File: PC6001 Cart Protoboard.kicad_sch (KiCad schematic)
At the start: 16 parts, among them J1 PC-6001 edge connector, SW1 PicoReset, SW2 EspReset, SW3 Button A, U2 ESP32-DevKitC, U3 74LS32, U4 microSD-Breakout

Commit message: oopsie on '08
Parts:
- removed unit 1 of U3
- added U5: 74LS08, Package_DIP:DIP-14_W7.62mm_Socket_LongPads, symbol 74xx:74LS08
- U3: footprint (none) -> Package_DIP:DIP-14_W7.62mm_Socket_LongPads
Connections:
- net +5V: now also U5.14 (VCC)
- net GND: now also U5.7 (GND)
- net ~{CS2}: now also U5.2
- net ~{CS3}: now also U5.1
- net ~{ROMSEL}: now also U5.3
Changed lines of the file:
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@@
 	)
 	(junction
+		(at 90.17 187.96)
+		(diameter 0)
+		(color 0 0 0 0)
+	)
+	(junction
 		(at 185.42 39.37)
 		(diameter 0)
@@
 	)
 	(junction
+		(at 90.17 162.56)
+		(diameter 0)
+		(color 0 0 0 0)
+	)
+	(junction
 		(at 226.06 53.34)
 		(diameter 0)
@@
 	(wire
 		(pts
+			(xy 69.85 187.96) (xy 90.17 187.96)
+		)
+		(stroke
+			(width 0)
+			(type default)
+		)
+	)
+	(wire
+		(pts
 			(xy 242.57 123.19) (xy 252.73 123.19)
 		)
@@
 	(wire
 		(pts
+			(xy 69.85 162.56) (xy 90.17 162.56)
+		)
+		(stroke
+			(width 0)
+			(type default)
+		)
+	)
+	(wire
+		(pts
 			(xy 177.8 29.21) (xy 185.42 29.21)
 		)
@@
 			)
 		)
-		(property "Footprint" ""
+		(property "Footprint" "Package_DIP:DIP-14_W7.62mm_Socket_LongPads"
 			(at 90.17 175.26 0)
 			(effects
@@
 	)
 	(symbol
+		(lib_id "74xx:74LS08")
+		(at 27.94 166.37 0)
+		(unit 1)
+		(exclude_from_sim no)
+		(in_bom yes)
+		(on_board yes)
+		(dnp no)
+		(fields_autoplaced yes)
+		(property "Reference" "U5"
+			(at 27.9317 157.48 0)
+			(effects
+				(font
+					(size 1.27 1.27)
+				)
+			)
+		)
+		(property "Value" "74LS08"
+			(at 27.9317 160.02 0)
+			(effects
+				(font
+					(size 1.27 1.27)
+				)
+			)
+		)
+		(property "Footprint" "Package_DIP:DIP-14_W7.62mm_Socket_LongPads"
+			(at 27.94 166.37 0)
+			(effects
+				(font
+					(size 1.27 1.27)
+				)
+				(hide yes)
+			)
+		)
+		(property "Datasheet" "http://www.ti.com/lit/gpn/sn74LS08"
+			(at 27.94 166.37 0)
+			(effects
+				(font
+					(size 1.27 1.27)
+				)
+				(hide yes)
+			)
+		)
+		(property "Description" "Quad And2"
+			(at 27.94 166.37 0)
+			(effects
+				(font
+					(size 1.27 1.27)
+				)
+				(hide yes)
+			)
+		)
+		(pin "1"
+		)
+		(pin "2"
+		)
+		(pin "3"
+		)
+		(pin "4"
+		)
+		(pin "5"
+		)
+		(pin "6"
+		)
+		(pin "10"
+		)
+		(pin "8"
+		)
+		(pin "9"
+		)
+		(pin "11"
+		)
+		(pin "12"
+		)
+		(pin "13"
+		)
+		(pin "14"
+		)
+		(pin "7"
+		)
+		(instances
+			(project ""
+				(path "/43e41326-819e-40e7-9c3a-9c7b5d01c509"
+					(reference "U5")
+					(unit 1)
+				)
+			)
+		)
+	)
+	(symbol
 		(lib_id "Device:R_Small_US")
 		(at 233.68 41.91 90)
@@
 	)
 	(symbol
-		(lib_id "74xx:74LS32")
-		(at 27.94 166.37 0)
-		(unit 1)
-		(exclude_from_sim no)
-		(in_bom yes)
-		(on_board yes)
-		(dnp no)
-		(fields_autoplaced yes)
-		(property "Reference" "U3"
-			(at 27.94 157.48 0)
-			(effects
-				(font
-					(size 1.27 1.27)
-				)
-			)
-		)
-		(property "Value" "74LS32"
-			(at 27.94 160.02 0)
-			(effects
-				(font
-					(size 1.27 1.27)
-				)
-			)
-		)
-		(property "Footprint" "Package_DIP:DIP-14_W7.62mm_LongPads"
-			(at 27.94 166.37 0)
-			(effects
-				(font
-					(size 1.27 1.27)
-				)
-				(hide yes)
-			)
-		)
-		(property "Datasheet" "http://www.ti.com/lit/gpn/sn74LS32"
-			(at 27.94 166.37 0)
-			(effects
-				(font
-					(size 1.27 1.27)
-				)
-				(hide yes)
-			)
-		)
-		(property "Description" "Quad 2-input OR"
-			(at 27.94 166.37 0)
-			(effects
-				(font
-					(size 1.27 1.27)
-				)
-				(hide yes)
-			)
-		)
-		(pin "14"
-		)
-		(pin "7"
-		)
-		(pin "8"
-		)
-		(pin "13"
-		)
-		(pin "5"
-		)
-		(pin "12"
-		)
-		(pin "4"
-		)
-		(pin "3"
-		)
-		(pin "11"
-		)
-		(pin "6"
-		)
-		(pin "10"
-		)
-		(pin "1"
-		)
-		(pin "9"
-		)
-		(pin "2"
-		)
-		(instances
-			(project ""
-				(path "/43e41326-819e-40e7-9c3a-9c7b5d01c509"
-					(reference "U3")
-					(unit 1)
-				)
-			)
-		)
-	)
-	(symbol
 		(lib_id "power:GND")
 		(at 33.02 144.78 0)
@@
 			)
 		)
-		(property "Footprint" ""
+		(property "Footprint" "Package_DIP:DIP-14_W7.62mm_Socket_LongPads"
 			(at 27.94 181.61 0)
 			(effects
@@
 				)
 			)
+		)
+	)
+	(symbol
+		(lib_id "74xx:74LS08")
+		(at 69.85 175.26 0)
+		(unit 5)
+		(exclude_from_sim no)
+		(in_bom yes)
+		(on_board yes)
+		(dnp no)
+		(fields_autoplaced yes)
+		(property "Reference" "U5"
+			(at 76.2 173.9899 0)
+			(effects
+				(font
+					(size 1.27 1.27)
+				)
+				(justify left)
+			)
+		)
+		(property "Value" "74LS08"
+			(at 76.2 176.5299 0)
+			(effects
+				(font
+					(size 1.27 1.27)
+				)
+				(justify left)
+			)
+		)
+		(property "Footprint" "Package_DIP:DIP-14_W7.62mm_Socket_LongPads"
+			(at 69.85 175.26 0)
+			(effects
+				(font
+					(size 1.27 1.27)
+				)
+				(hide yes)
+			)
+		)
+		(property "Datasheet" "http://www.ti.com/lit/gpn/sn74LS08"
+			(at 69.85 175.26 0)
+			(effects
+				(font
+					(size 1.27 1.27)
+				)
+				(hide yes)
+			)
+		)
+		(property "Description" "Quad And2"
+			(at 69.85 175.26 0)
+			(effects
+				(font
+					(size 1.27 1.27)
+				)
+				(hide yes)
+			)
+		)
+		(pin "2"
+		)
+		(pin "1"
+		)
+		(pin "9"
+		)
+		(pin "11"
+		)
+		(pin "10"
+		)
+		(pin "8"
+		)
+		(pin "5"
+		)
+		(pin "12"
+		)
+		(pin "13"
+		)
+		(pin "14"
+		)
+		(pin "7"
+		)
+		(pin "3"
+		)
+		(pin "6"
+		)
+		(pin "4"
+		)
+		(instances
+			(project ""
+				(path "/43e41326-819e-40e7-9c3a-9c7b5d01c509"
+					(reference "U5")
+					(unit 5)
+				)
+			)

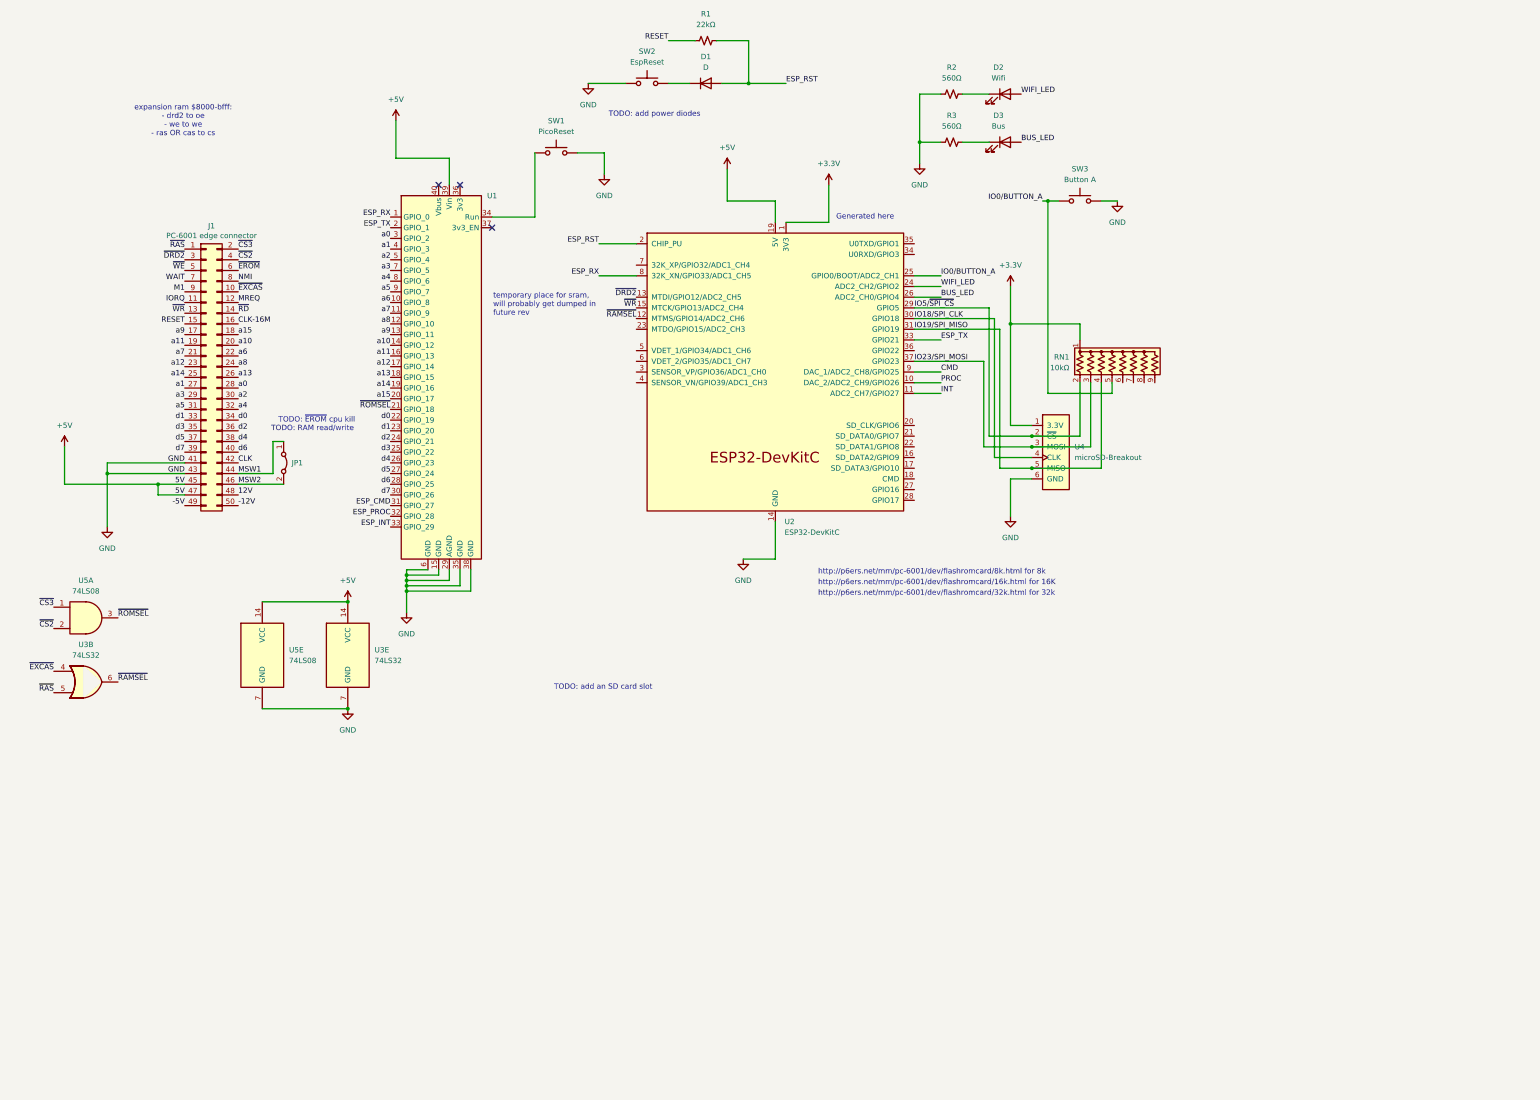
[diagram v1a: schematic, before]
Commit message: Make schematic larger to prepare for buffers
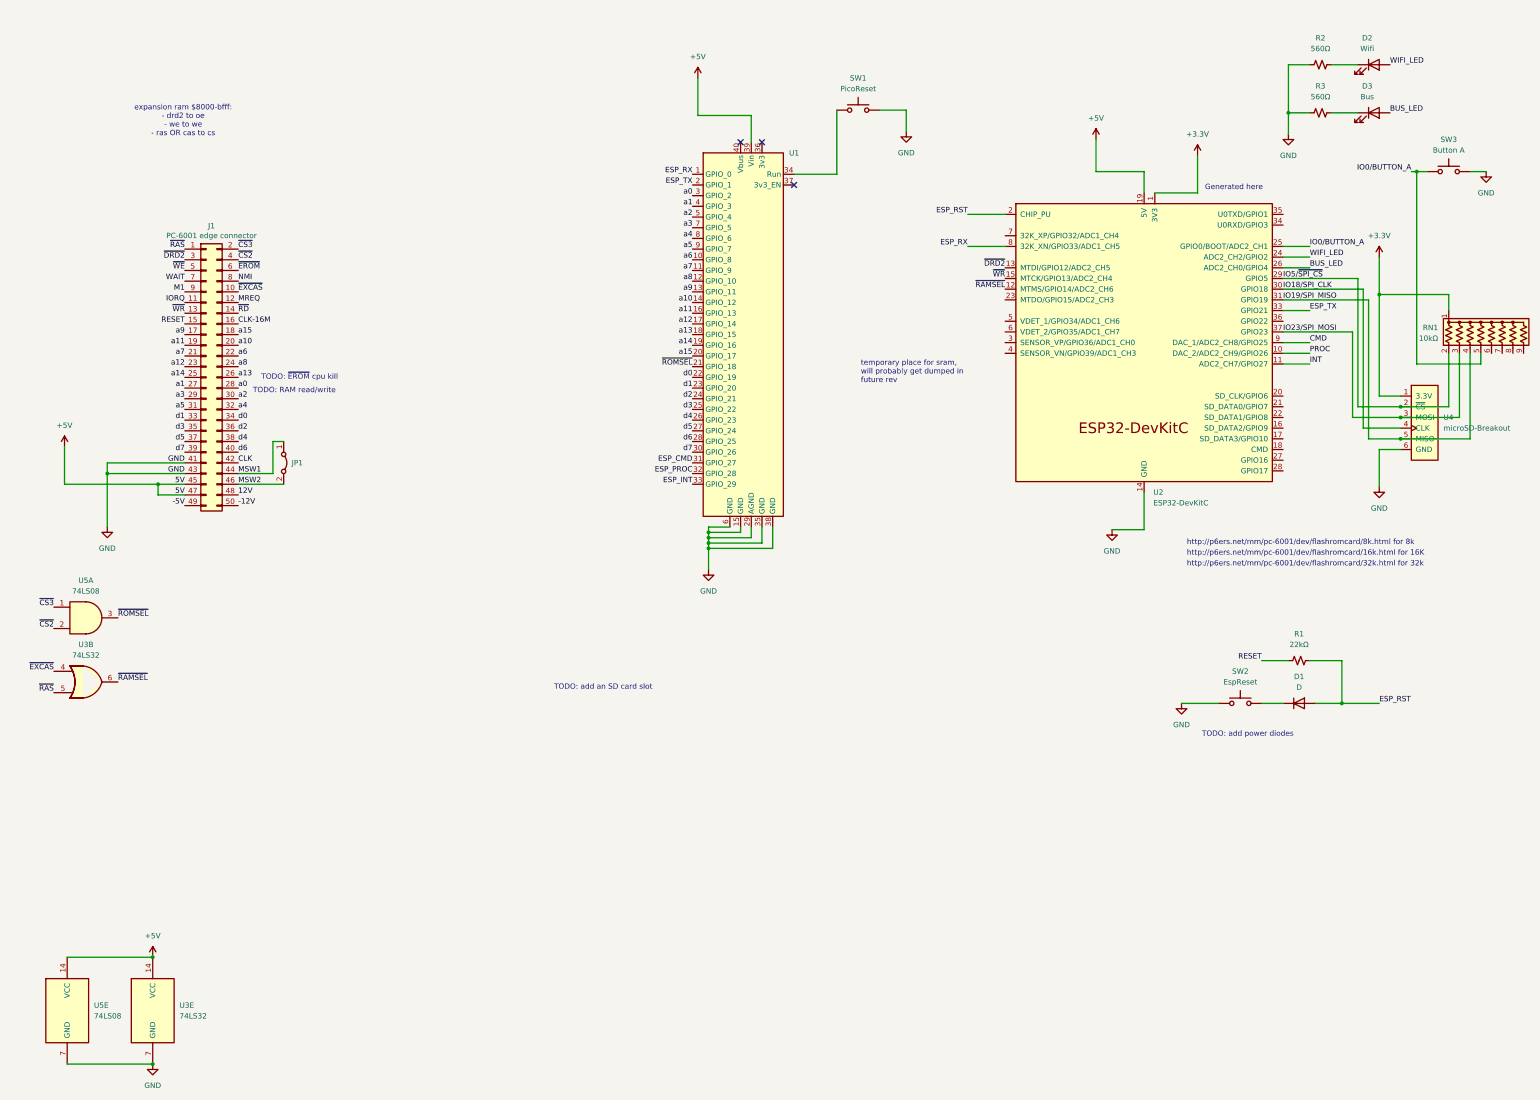
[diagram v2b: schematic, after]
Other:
- moved on the sheet: D1, D2, D3, R1, R2, R3, RN1, SW1, SW2, SW3, U1, U2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

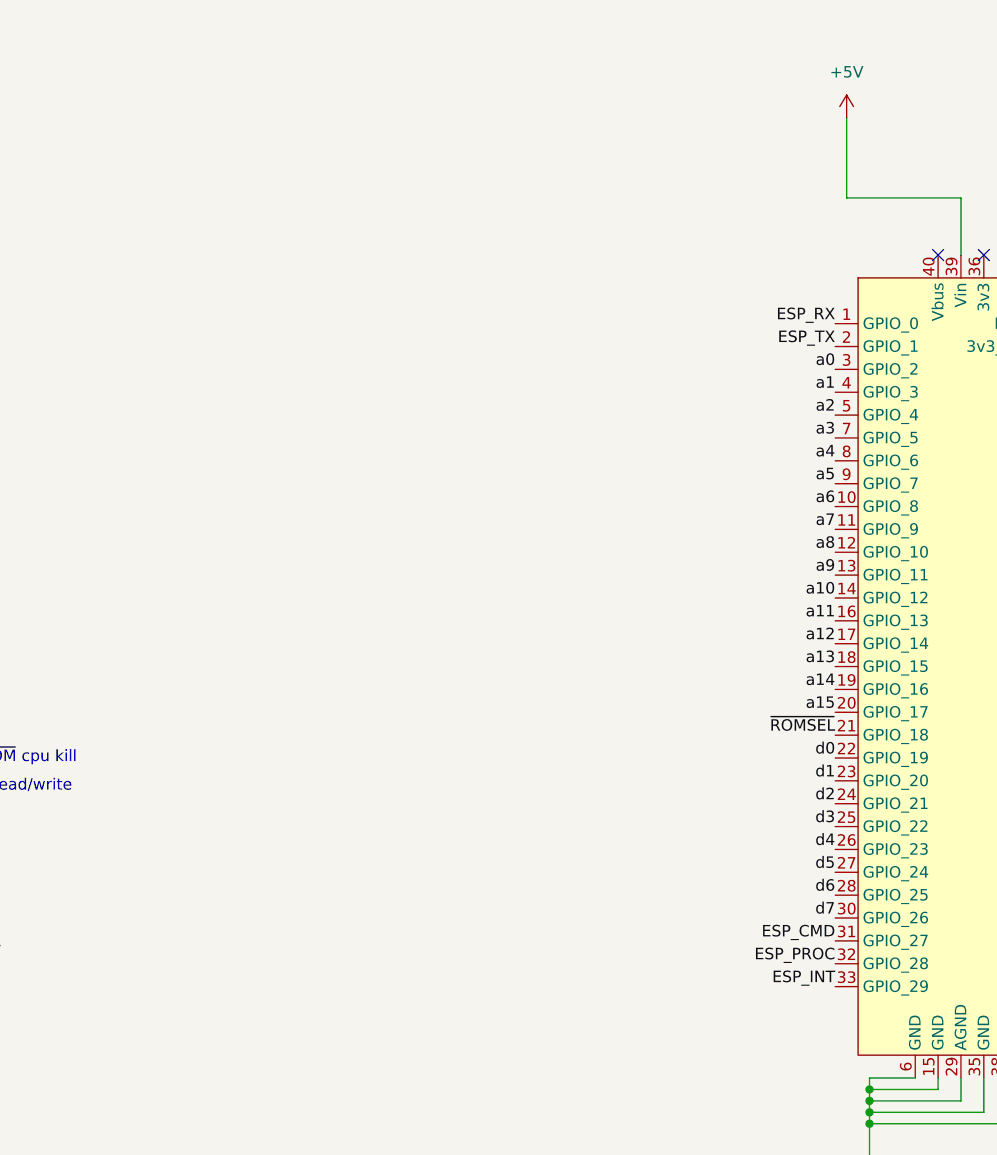
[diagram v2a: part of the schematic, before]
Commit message: Sketching out modified 74lvc245
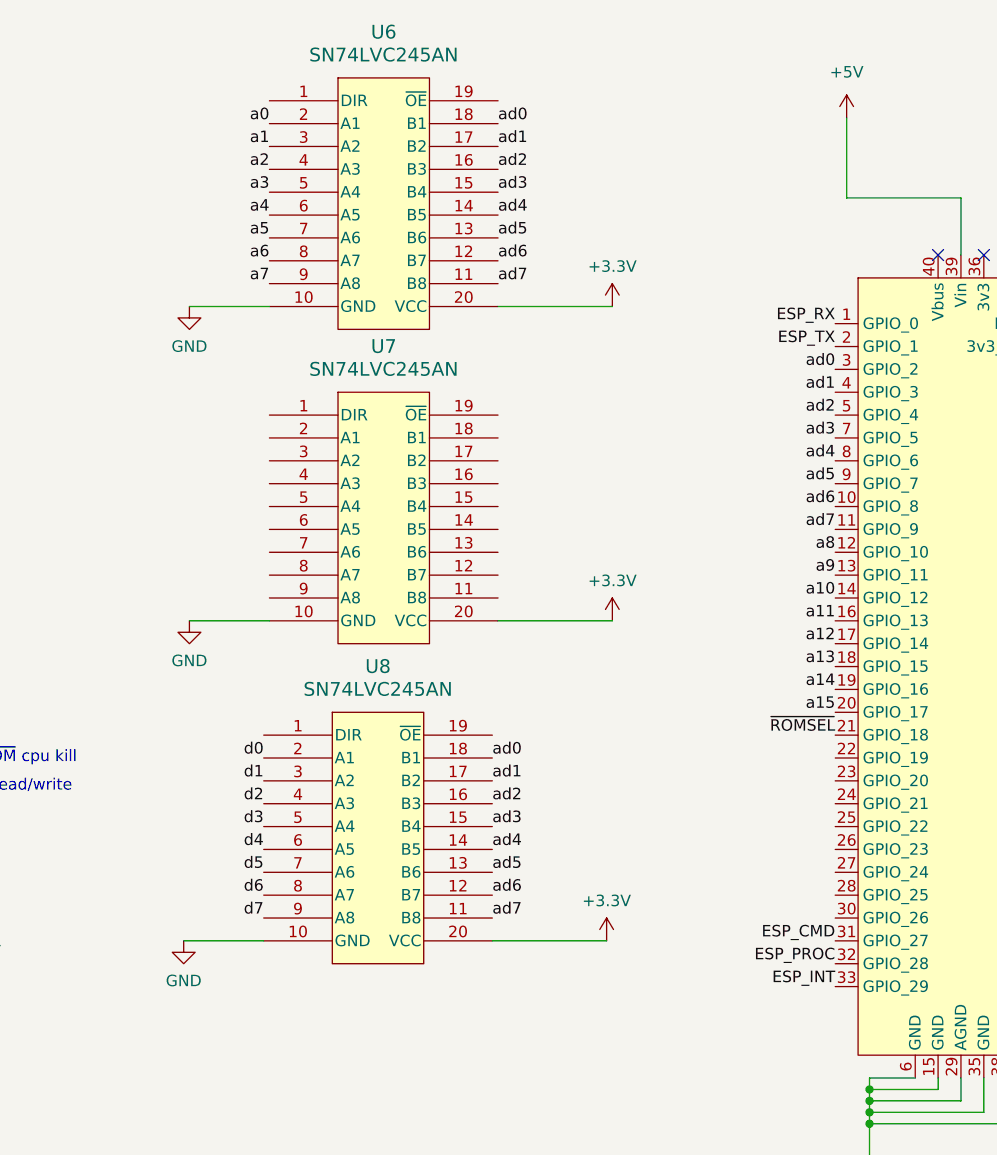
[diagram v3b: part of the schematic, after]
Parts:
- added U6, U7, U8: SN74LVC245AN, Package_DIP:DIP-20_W7.62mm_Socket_LongPads, symbol 74lvc245an:SN74LVC245AN
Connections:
- net +3.3V: now also U6.20 (VCC), U7.20 (VCC), U8.20 (VCC)
- net GND: now also U6.10 (GND), U7.10 (GND), U8.10 (GND)
- net a0: now also U6.2 (A1); no longer U1.3 (GPIO_2)
- net a1: now also U6.3 (A2); no longer U1.4 (GPIO_3)
- net a2: now also U6.4 (A3); no longer U1.5 (GPIO_4)
- net a3: now also U6.5 (A4); no longer U1.7 (GPIO_5)
- net a4: now also U6.6 (A5); no longer U1.8 (GPIO_6)
- net a5: now also U6.7 (A6); no longer U1.9 (GPIO_7)
- net a6: now also U6.8 (A7); no longer U1.10 (GPIO_8)
- net a7: now also U6.9 (A8); no longer U1.11 (GPIO_9)
- net d0: now also U8.2 (A1); no longer U1.22 (GPIO_19)
- net d1: now also U8.3 (A2); no longer U1.23 (GPIO_20)
- net d2: now also U8.4 (A3); no longer U1.24 (GPIO_21)
- net d3: now also U8.5 (A4); no longer U1.25 (GPIO_22)
- net d4: now also U8.6 (A5); no longer U1.26 (GPIO_23)
- net d5: now also U8.7 (A6); no longer U1.27 (GPIO_24)
- net d6: now also U8.8 (A7); no longer U1.28 (GPIO_25)
- net d7: now also U8.9 (A8); no longer U1.30 (GPIO_26)
- new net ad0: U1.3 (GPIO_2), U6.18 (B1), U8.18 (B1)
- new net ad1: U1.4 (GPIO_3), U6.17 (B2), U8.17 (B2)
- new net ad2: U1.5 (GPIO_4), U6.16 (B3), U8.16 (B3)
- new net ad3: U1.7 (GPIO_5), U6.15 (B4), U8.15 (B4)
- new net ad4: U1.8 (GPIO_6), U6.14 (B5), U8.14 (B5)
- new net ad5: U1.9 (GPIO_7), U6.13 (B6), U8.13 (B6)
- new net ad6: U1.10 (GPIO_8), U6.12 (B7), U8.12 (B7)
- new net ad7: U1.11 (GPIO_9), U6.11 (B8), U8.11 (B8)
